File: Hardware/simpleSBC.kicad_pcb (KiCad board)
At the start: 6 copper layers, 82.7 x 56 mm, 201 parts, among them J1 Conn_02x07_Odd_Even, J2 Micro_SD_Card_Det2, J4 Barrel_Jack_Switch, J5 USB_A, J6 USB_A, J7 RJ45_Wuerth_7499010121A, J8 Conn_01x03, J9 Conn_01x06, SW1 SW_Push, U1 STM32MP157FAD1, U2 STMPS2252MTR, U3 MT41K256M16TW, U4 STPMIC1, U5 USBLC6-4SC6, U6 LAN8742A, X1 ASCO, Y1 32.786, Y3 24M

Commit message: ERC/DRC Clean
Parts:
- added J3: Conn_02x10_Odd_Even, Connector_PinHeader_2.54mm:PinHeader_2x10_P2.54mm_Vertical, F.Cu at (170.5, 88.6)
- J9: value Conn_01x06 -> Conn_02x10_Odd_Even; footprint Connector_PinHeader_2.54mm:PinHeader_1x06_P2.54mm_Vertical -> Connector_PinHeader_2.54mm:PinHeader_2x10_P2.54mm_Vertical
- moved J9 24.8 mm to (179.7, 88.6)
- moved C9 0.74 mm to (120.5, 79.2), turned to 90 degrees
- moved JP6 0.50 mm to (125.0, 73.2)
- moved R55 0.22 mm to (159.5, 74.2)
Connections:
- J9 pad 1: /IO1 -> /PA15
- J9 pad 2: /IO2 -> /PC7
- J9 pad 3: /IO3 -> /PE2
- J9 pad 4: /IO4 -> /PC2
- J9 pad 5: /IO5 -> /PG10
- J9 pad 6: /IO6 -> /PD15
- JP7 pad 1: unconnected-(JP7-A-Pad1) -> /VBUS1
- JP7 pad 3: unconnected-(JP7-B-Pad3) -> /PMIC_VBUSOTG
- U1 pad 1C2: unconnected-(U1B-PD15-Pad1C2) -> /PD15
- U1 pad A2: unconnected-(U1B-PD1-PadA2) -> /PD1
- U1 pad A4: unconnected-(U1B-PC6-PadA4) -> /PC6
- U1 pad A7: unconnected-(U1B-PD3-PadA7) -> /PD3
- U1 pad B1: unconnected-(U1B-PG15-PadB1) -> /PG15
- U1 pad B18: /Memory/UDQS- -> /Memory/LDQS-
- U1 pad B19: /Memory/UDQS+ -> /Memory/LDQS+
- U1 pad B2: unconnected-(U1B-PE6-PadB2) -> /PE6
- U1 pad B3: unconnected-(U1B-PD7-PadB3) -> /PD7
- U1 pad B4: unconnected-(U1B-PA15-PadB4) -> /PA15
- U1 pad B5: unconnected-(U1B-PG6-PadB5) -> /PG6
- U1 pad B6: unconnected-(U1B-PB4-PadB6) -> /PB4
- U1 pad B7: unconnected-(U1B-PE5-PadB7) -> /PE5
- U1 pad B8: unconnected-(U1B-PA8-PadB8) -> /PA8
- U1 pad C1: unconnected-(U1B-PE12-PadC1) -> /PE12
- U1 pad C10: unconnected-(U1B-PC7-PadC10) -> /PC7
- U1 pad C17: /Memory/UDM -> /Memory/LDM
- U1 pad C2: unconnected-(U1B-PE0-PadC2) -> /PE0
- U1 pad C3: unconnected-(U1B-PD4-PadC3) -> /PD4
- U1 pad C4: unconnected-(U1B-PD5-PadC4) -> /PD5
- U1 pad C5: unconnected-(U1B-PD0-PadC5) -> /PD0
- U1 pad C6: unconnected-(U1B-PA9-PadC6) -> /PA9
- U1 pad C8: unconnected-(U1B-PB15-PadC8) -> /PB15
- U1 pad C9: unconnected-(U1B-PB9-PadC9) -> /PB9
- U1 pad D1: unconnected-(U1B-PG12-PadD1) -> /PG12
- U1 pad D3: unconnected-(U1B-PE15-PadD3) -> /PE15
- U1 pad E1: unconnected-(U1B-PD8-PadE1) -> /PD8
- U1 pad E3: unconnected-(U1B-PE13-PadE3) -> /PE13
- U1 pad P1: unconnected-(U1B-PE2-PadP1) -> /PE2
- U1 pad P2: unconnected-(U1B-PC2-PadP2) -> /PC2
- U1 pad U1: unconnected-(U1B-PB1-PadU1) -> /PB1
- U1 pad U18: /Memory/LDQS- -> /Memory/UDQS-
- U1 pad U2: unconnected-(U1B-PB0-PadU2) -> /PB0
- U1 pad U4: unconnected-(U1B-PC0-PadU4) -> /PC0
- U1 pad U7: unconnected-(U1B-PG10-PadU7) -> /PG10
- U1 pad U8: unconnected-(U1B-PD11-PadU8) -> /PD11
- U1 pad V18: /Memory/LDM -> /Memory/UDM
- U1 pad V19: /Memory/LDQS+ -> /Memory/UDQS+
- U1 pad V3: unconnected-(U1B-PB12-PadV3) -> /PB12
- U1 pad V4: unconnected-(U1B-PB8-PadV4) -> /PB8
- U1 pad W3: /IO3 -> /PA6
- U1 pad W4: /IO4 -> /PF11
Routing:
- net GND: track 137.2 -> 210.7 mm, vias 70 -> 90
- net /PMIC_VBUSOTG: track 1.12 -> 73.1 mm, vias 0 -> 3
- net /PC7: track 0.00 -> 70.0 mm, vias 0 -> 2
- net /PG6: track 0.00 -> 52.3 mm, vias 0 -> 1
- net /PD3: track 0.00 -> 49.5 mm, vias 0 -> 1
- net /PE5: track 0.00 -> 47.2 mm, vias 0 -> 1
- net /PB4: track 0.00 -> 46.9 mm, vias 0 -> 1
- net /PD15: track 0.00 -> 43.8 mm, vias 0 -> 1
- net /PD0: track 0.00 -> 43.5 mm, vias 0 -> 1
- net /PA15: track 0.00 -> 43.0 mm, vias 0 -> 2
- net /VBUS1: track 0.00 -> 41.7 mm, vias 0 -> 2
- net /PC2: track 0.00 -> 41.3 mm, vias 0 -> 1
- net /PG10: track 0.00 -> 40.4 mm, vias 0 -> 1
- net /PD1: track 0.00 -> 39.7 mm, vias 0 -> 2
- net /PD5: track 0.00 -> 39.4 mm, vias 0 -> 1
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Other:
- outline, holes or cut-outs redrawn
- board text added: "5V IN"
- board text added: "GND"
- board text added: "PA13"
- board text added: "PA14"
- board text added: "RESET"
- board text added: "SCL"
- board text added: "SDA"
- board text added: "ST-Link"
- board text removed: "VDD_USB?"

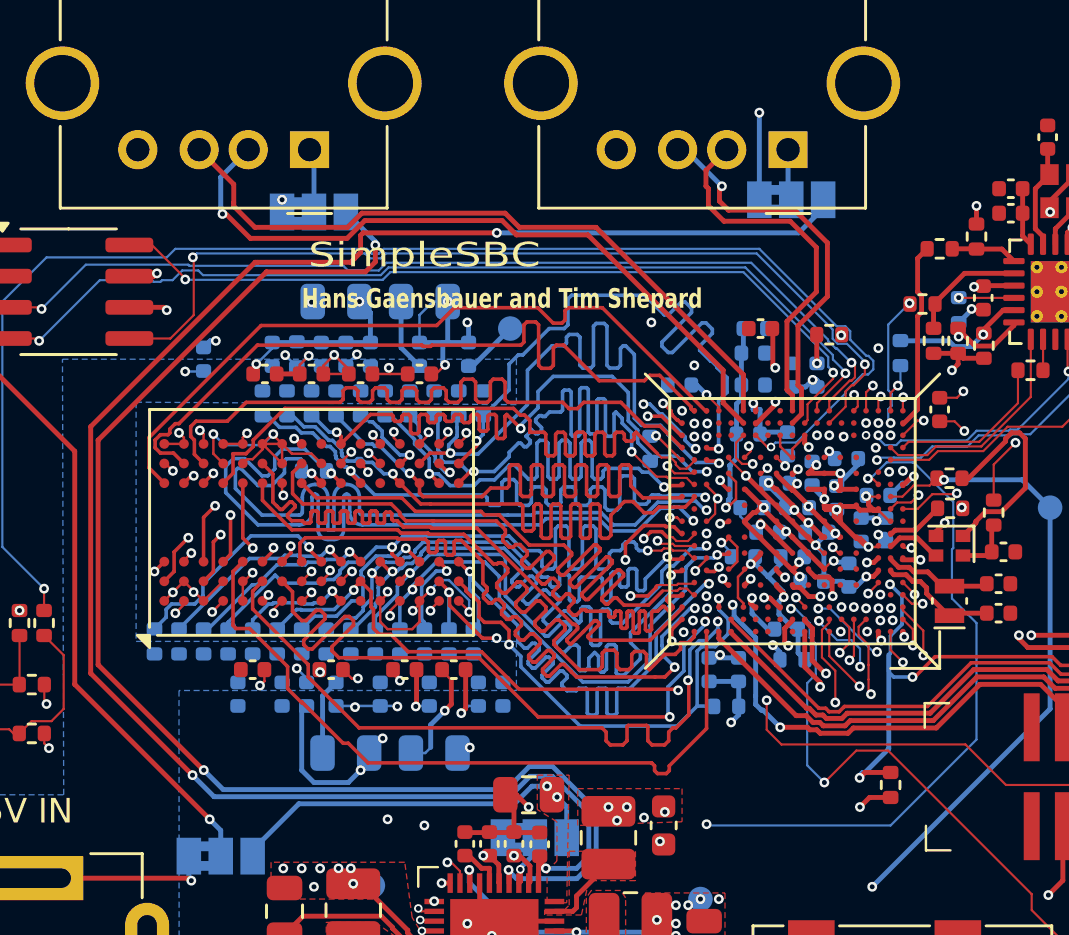
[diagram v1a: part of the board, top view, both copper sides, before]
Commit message: Redo DRAM Length Tuning
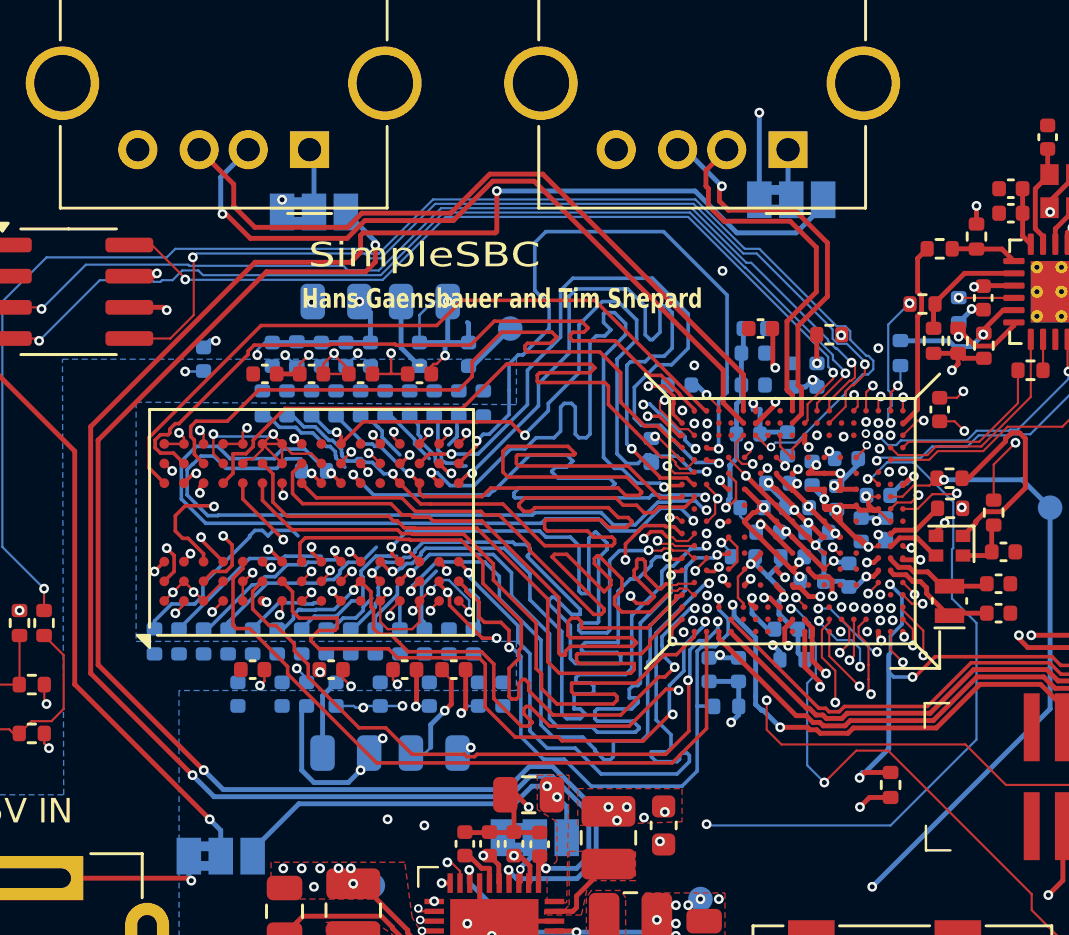
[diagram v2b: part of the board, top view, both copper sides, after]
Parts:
- moved R3 0.10 mm to (138.8, 83.0)
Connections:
- J9 pad 5: /PG10 -> /PA4
- U1 pad 1J1: unconnected-(U1B-PA4-Pad1J1) -> /PA4
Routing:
- net /PG10: track 40.4 -> 0.00 mm, vias 1 -> 0
- net /PA4: track 0.00 -> 40.4 mm, vias 0 -> 1
- net unconnected-(J7-PadSH)_1: track 15.8 -> 0.00 mm
- net unconnected-(J7-PadSH): track 0.00 -> 15.8 mm
- net /Memory/A7: track 15.9 -> 28.4 mm
- net /Memory/A5: track 21.8 -> 28.0 mm
- net /Memory/~{RESET}: track 20.0 -> 25.3 mm
- net /Memory/A11: track 24.3 -> 29.4 mm
- net /Memory/A12: track 31.2 -> 36.1 mm
- net /Memory/A1: track 29.6 -> 34.5 mm
- net /Memory/UDM: track 32.9 -> 28.3 mm
- net /Memory/A0: track 30.4 -> 34.6 mm
- net /Memory/BA0: track 25.3 -> 29.3 mm
- net /Memory/~{CS}: track 29.2 -> 32.9 mm
- net /Memory/DQ11: track 31.8 -> 28.2 mm
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
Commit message: Reconnect Nets after length tuning
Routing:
- net unconnected-(J7-PadSH): track 15.8 -> 0.00 mm
- net GND: track 210.5 -> 214.1 mm, vias 89 -> 90
- net /Memory/A7: track 28.4 -> 29.9 mm
- net /Memory/BA0: track 29.3 -> 30.3 mm
- net /Memory/A13: track 28.6 -> 29.5 mm
- net /Memory/A6: track 32.6 -> 31.7 mm
- net /Memory/BA2: track 29.1 -> 29.9 mm
- net /Memory/A3: track 29.0 -> 29.8 mm
- net /Memory/A8: track 27.4 -> 28.1 mm
- net /Memory/~{CAS}: track 39.7 -> 40.4 mm
- net /Memory/ODT: track 31.9 -> 32.5 mm
- net /Memory/A5: track 28.0 -> 28.7 mm
- net /Memory/A0: track 34.6 -> 35.2 mm
- net /Memory/A11: track 29.4 -> 30.0 mm
- net /Memory/~{RAS}: track 36.7 -> 37.3 mm
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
